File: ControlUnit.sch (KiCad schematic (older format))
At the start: 51 parts, among them SW1 SW_Push-Switch, U19 7400, U20 74LS161-74xx, U21 AT28C256, U22 AT28C256, U23 74LS138, U24 74LS138, U25 74LS138

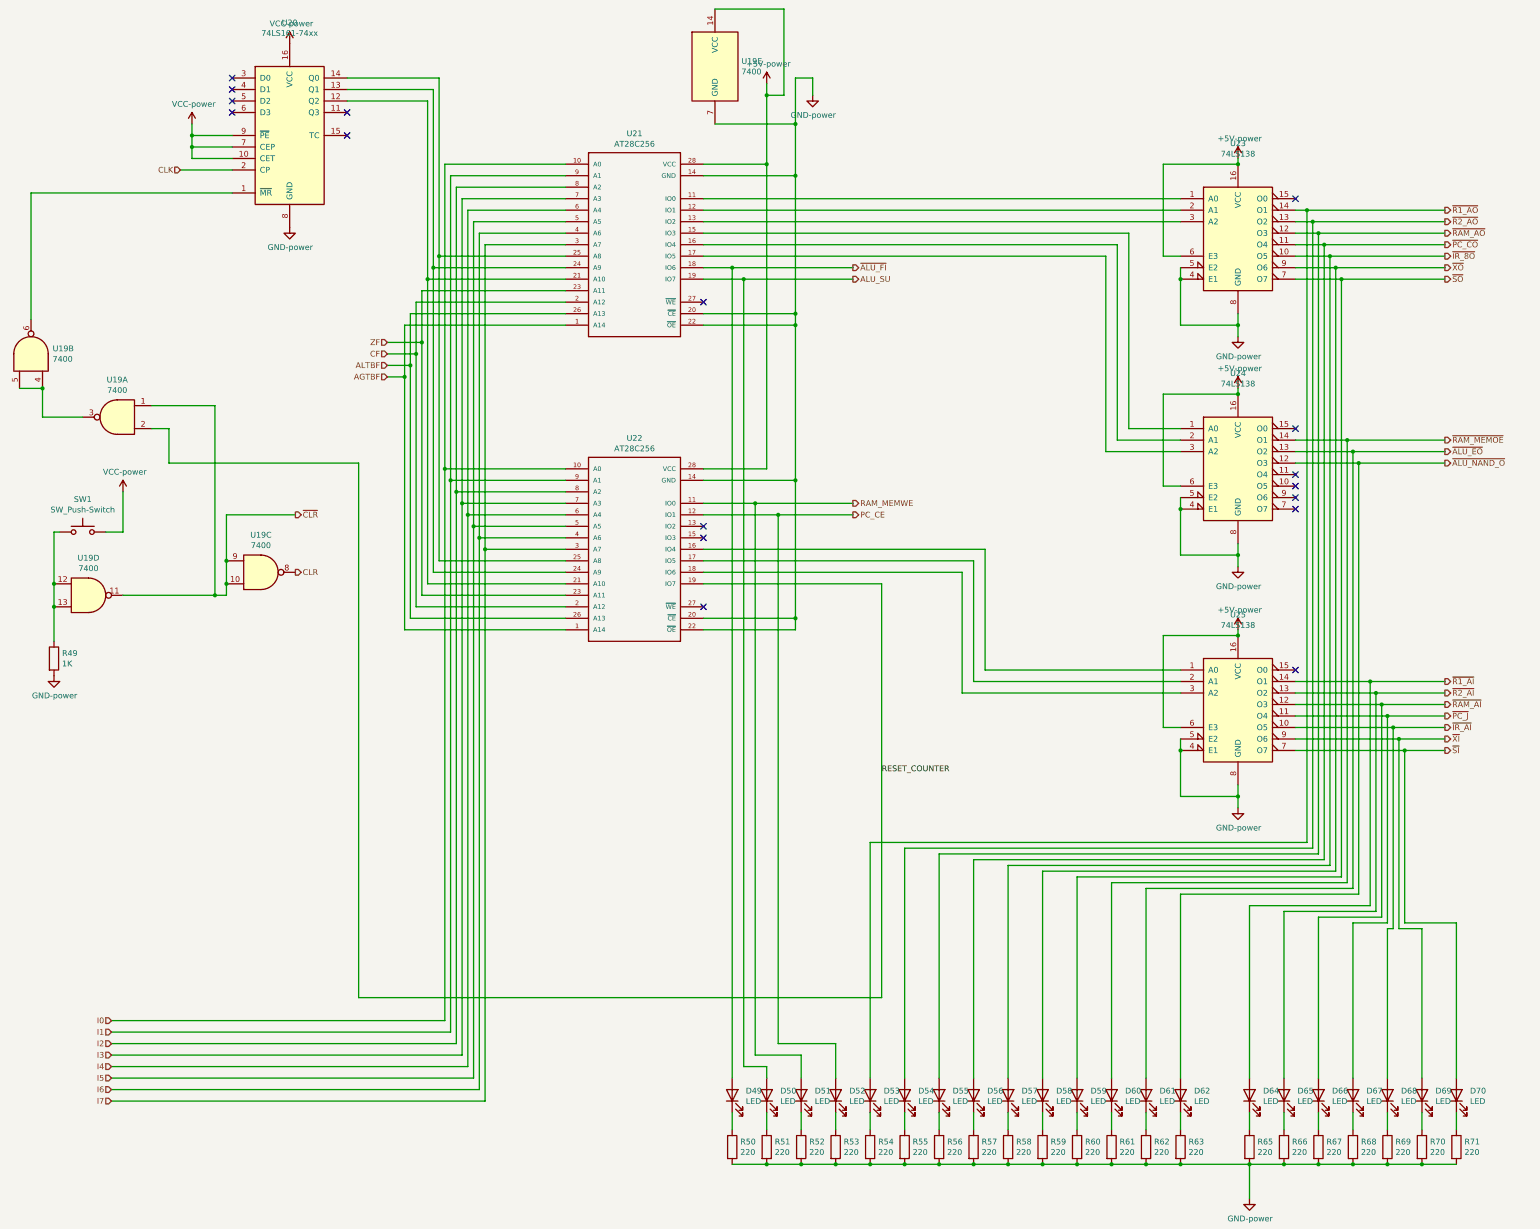
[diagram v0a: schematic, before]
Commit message: added images,fixed readme,renamed stuff to not include spaces
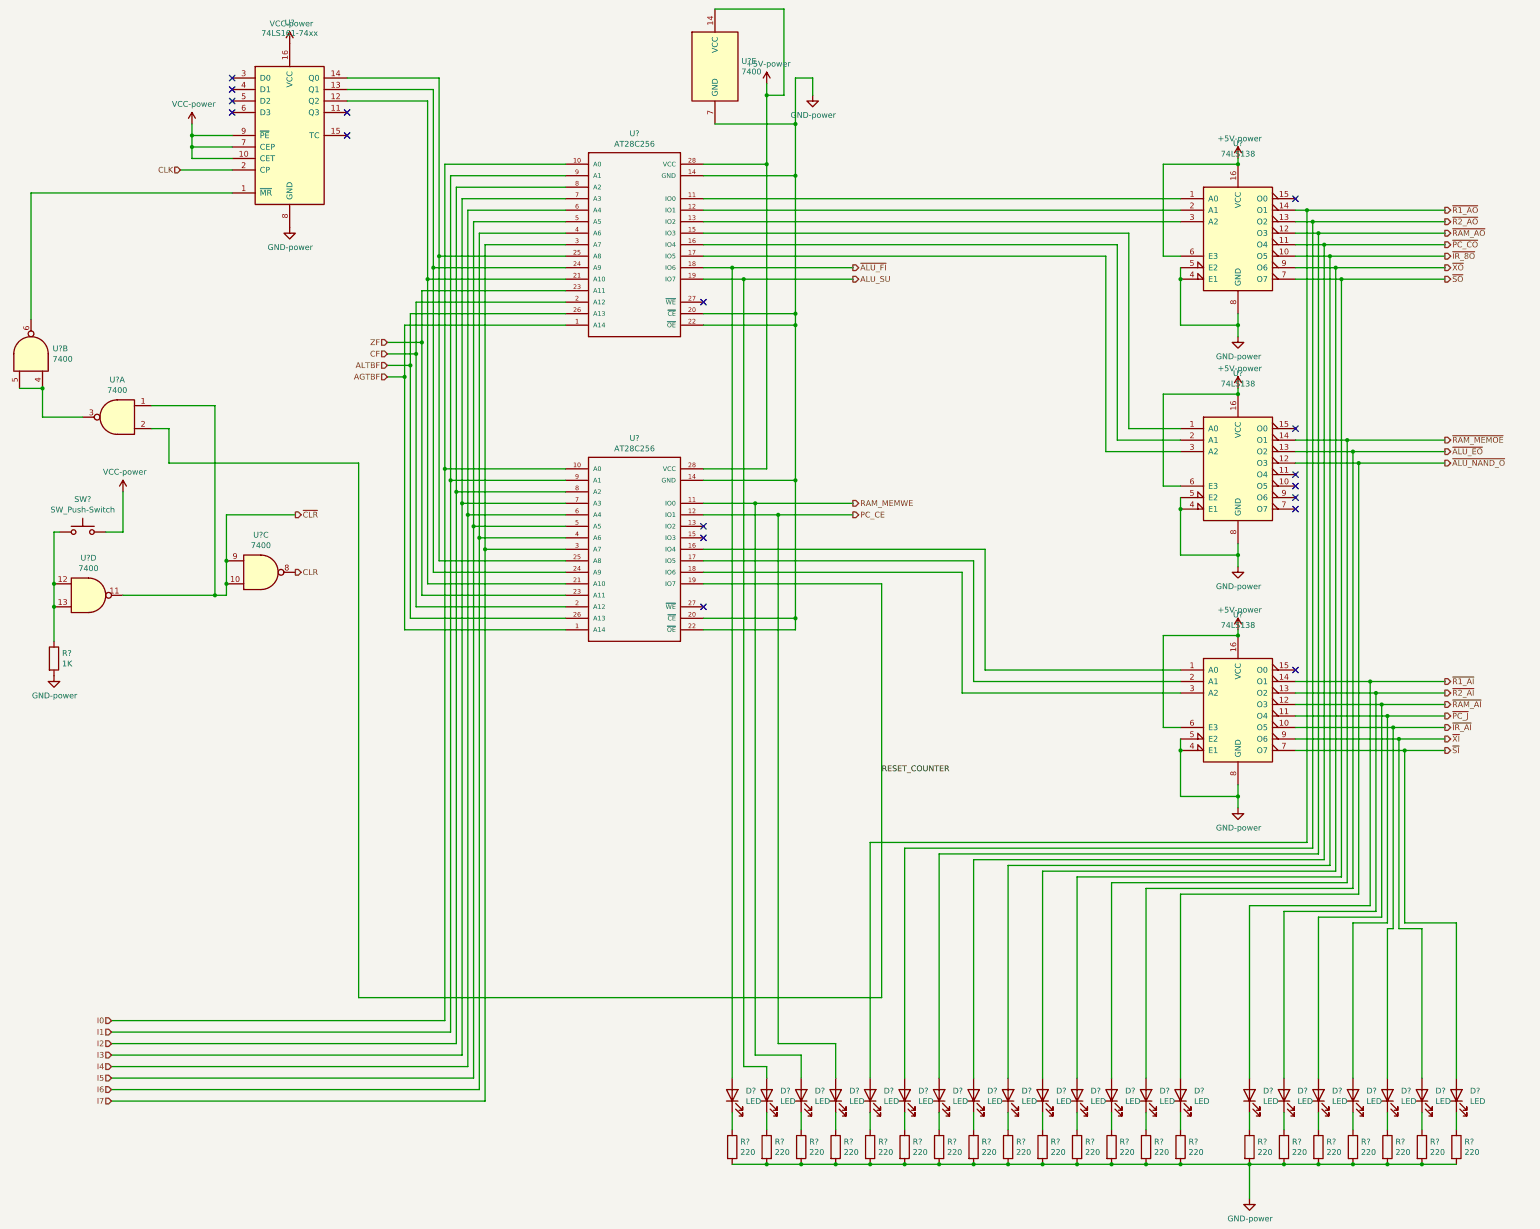
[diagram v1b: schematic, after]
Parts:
- renumbered R49 to R?, SW1 to SW?, U20 to U?, U19 to U?, U21 to U?, U22 to U?, U23 to U?, U25 to U?, U24 to U?

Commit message: added power caps
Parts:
- added C28, C29, C30, C31: 0.1uF, Capacitor_THT:CP_Axial_L10.0mm_D4.5mm_P15.00mm_Horizontal, symbol Device:C
- gave numbers to parts that had none: 9
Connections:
- net GND: now also C28.2, C29.2, C30.2, C31.2
- net VCC: now also C28.1, C29.1, C30.1, C31.1

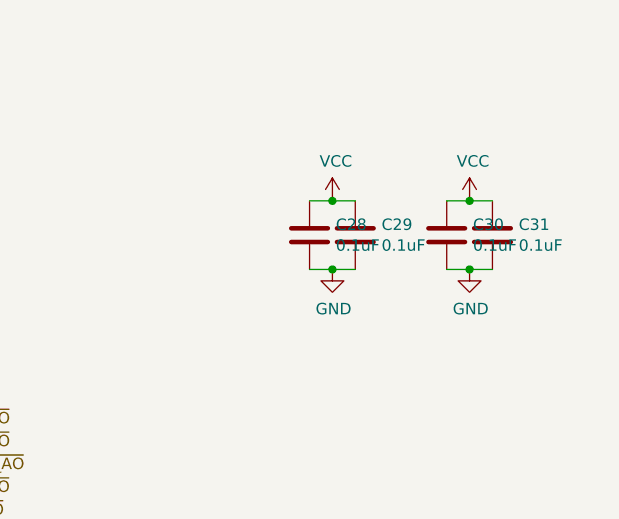
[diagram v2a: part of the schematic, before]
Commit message: Added power connector
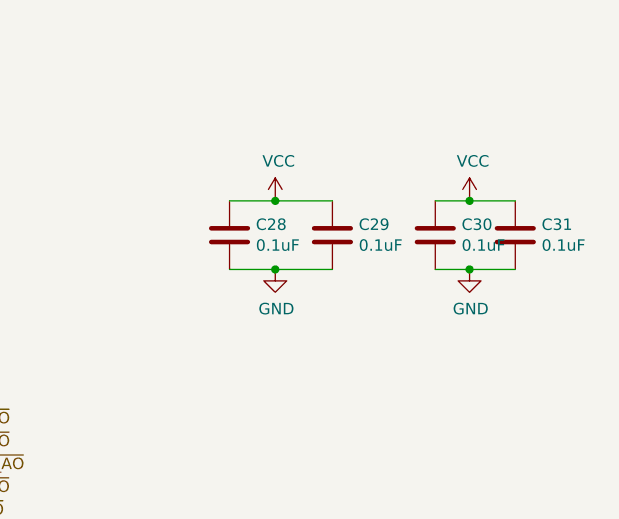
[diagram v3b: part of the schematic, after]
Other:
- moved on the sheet: C28, C29, C30, C31
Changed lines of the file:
@@
 $Descr A2 23386 16535
 encoding utf-8
-Sheet 21 21
+Sheet 21 22
 Title ""
 Date ""
@@
 L 16bitCpu-rescue:VCC-power #PWR?
 U 1 1 5FD5AD5A
-P 15300 1750
+P 15050 1750
 AR Path="/5FD5AD5A" Ref="#PWR?"  Part="1"
 AR Path="/5FD099BF/5FD5AD5A" Ref="#PWR0294"  Part="1"
-F 0 "#PWR0294" H 15300 1600 50  0001 C CNN
-F 1 "VCC" H 15315 1923 50  0000 C CNN
-F 2 "" H 15300 1750 50  0001 C CNN
-F 3 "" H 15300 1750 50  0001 C CNN
-	1    15300 1750
+F 0 "#PWR0294" H 15050 1600 50  0001 C CNN
+F 1 "VCC" H 15065 1923 50  0000 C CNN
+F 2 "" H 15050 1750 50  0001 C CNN
+F 3 "" H 15050 1750 50  0001 C CNN
+	1    15050 1750
 	1    0    0    -1
 $EndComp
@@
 L 16bitCpu-rescue:GND-power #PWR?
 U 1 1 5FD5AD60
-P 15300 2050
+P 15050 2050
 AR Path="/5FD5AD60" Ref="#PWR?"  Part="1"
 AR Path="/5F75E433/5FD5AD60" Ref="#PWR?"  Part="1"
 AR Path="/5FD099BF/5FD5AD60" Ref="#PWR0295"  Part="1"
-F 0 "#PWR0295" H 15300 1800 50  0001 C CNN
-F 1 "GND" H 15305 1877 50  0000 C CNN
-F 2 "" H 15300 2050 50  0001 C CNN
-F 3 "" H 15300 2050 50  0001 C CNN
-	1    15300 2050
-	1    0    0    -1
-$EndComp
-Wire Wire Line
-	15300 1750 15400 1750
-Wire Wire Line
-	15400 2050 15300 2050
+F 0 "#PWR0295" H 15050 1800 50  0001 C CNN
+F 1 "GND" H 15055 1877 50  0000 C CNN
+F 2 "" H 15050 2050 50  0001 C CNN
+F 3 "" H 15050 2050 50  0001 C CNN
+	1    15050 2050
+	1    0    0    -1
+$EndComp
 $Comp
 L Device:C C?
 U 1 1 5FD5AD68
-P 15200 1900
+P 14850 1900
 AR Path="/5F75E433/5FD5AD68" Ref="C?"  Part="1"
 AR Path="/5FD099BF/5FD5AD68" Ref="C28"  Part="1"
-F 0 "C28" H 15315 1946 50  0000 L CNN
-F 1 "0.1uF" H 15315 1855 50  0000 L CNN
-F 2 "Capacitor_THT:CP_Axial_L10.0mm_D4.5mm_P15.00mm_Horizontal" H 15238 1750 50  0001 C CNN
-F 3 "" H 15200 1900 50  0001 C CNN
-	1    15200 1900
-	1    0    0    -1
-$EndComp
-Wire Wire Line
-	15300 1750 15200 1750
-Connection ~ 15300 1750
-Wire Wire Line
-	15200 2050 15300 2050
-Connection ~ 15300 2050
+F 0 "C28" H 14965 1946 50  0000 L CNN
+F 1 "0.1uF" H 14965 1855 50  0000 L CNN
+F 2 "Capacitor_THT:CP_Axial_L10.0mm_D4.5mm_P15.00mm_Horizontal" H 14888 1750 50  0001 C CNN
+F 3 "" H 14850 1900 50  0001 C CNN
+	1    14850 1900
+	1    0    0    -1
+$EndComp
+Connection ~ 15050 1750
+Connection ~ 15050 2050
 $Comp
 L Device:C C?
 U 1 1 5FD5AD72
-P 15400 1900
+P 15300 1900
 AR Path="/5F75E433/5FD5AD72" Ref="C?"  Part="1"
 AR Path="/5FD099BF/5FD5AD72" Ref="C29"  Part="1"
-F 0 "C29" H 15515 1946 50  0000 L CNN
-F 1 "0.1uF" H 15515 1855 50  0000 L CNN
-F 2 "Capacitor_THT:CP_Axial_L10.0mm_D4.5mm_P15.00mm_Horizontal" H 15438 1750 50  0001 C CNN
-F 3 "" H 15400 1900 50  0001 C CNN
-	1    15400 1900
+F 0 "C29" H 15415 1946 50  0000 L CNN
+F 1 "0.1uF" H 15415 1855 50  0000 L CNN
+F 2 "Capacitor_THT:CP_Axial_L10.0mm_D4.5mm_P15.00mm_Horizontal" H 15338 1750 50  0001 C CNN
+F 3 "" H 15300 1900 50  0001 C CNN
+	1    15300 1900
 	1    0    0    -1
 $EndComp
@@
 	1    0    0    -1
 $EndComp
-Wire Wire Line
-	15900 1750 16000 1750
-Wire Wire Line
-	16000 2050 15900 2050
 $Comp
 L Device:C C?
 U 1 1 5FD78AFF
-P 15800 1900
+P 15750 1900
 AR Path="/5F75E433/5FD78AFF" Ref="C?"  Part="1"
 AR Path="/5FD099BF/5FD78AFF" Ref="C30"  Part="1"
-F 0 "C30" H 15915 1946 50  0000 L CNN
-F 1 "0.1uF" H 15915 1855 50  0000 L CNN
-F 2 "Capacitor_THT:CP_Axial_L10.0mm_D4.5mm_P15.00mm_Horizontal" H 15838 1750 50  0001 C CNN
-F 3 "" H 15800 1900 50  0001 C CNN
-	1    15800 1900
-	1    0    0    -1
-$EndComp
-Wire Wire Line
-	15900 1750 15800 1750
+F 0 "C30" H 15865 1946 50  0000 L CNN
+F 1 "0.1uF" H 15865 1855 50  0000 L CNN
+F 2 "Capacitor_THT:CP_Axial_L10.0mm_D4.5mm_P15.00mm_Horizontal" H 15788 1750 50  0001 C CNN
+F 3 "" H 15750 1900 50  0001 C CNN
+	1    15750 1900
+	1    0    0    -1
+$EndComp
 Connection ~ 15900 1750
-Wire Wire Line
-	15800 2050 15900 2050
 Connection ~ 15900 2050
 $Comp
 L Device:C C?
 U 1 1 5FD78B09
-P 16000 1900
+P 16100 1900
 AR Path="/5F75E433/5FD78B09" Ref="C?"  Part="1"
 AR Path="/5FD099BF/5FD78B09" Ref="C31"  Part="1"
-F 0 "C31" H 16115 1946 50  0000 L CNN
-F 1 "0.1uF" H 16115 1855 50  0000 L CNN
-F 2 "Capacitor_THT:CP_Axial_L10.0mm_D4.5mm_P15.00mm_Horizontal" H 16038 1750 50  0001 C CNN
-F 3 "" H 16000 1900 50  0001 C CNN
-	1    16000 1900
-	1    0    0    -1
-$EndComp
+F 0 "C31" H 16215 1946 50  0000 L CNN
+F 1 "0.1uF" H 16215 1855 50  0000 L CNN
+F 2 "Capacitor_THT:CP_Axial_L10.0mm_D4.5mm_P15.00mm_Horizontal" H 16138 1750 50  0001 C CNN
+F 3 "" H 16100 1900 50  0001 C CNN
+	1    16100 1900
+	1    0    0    -1
+$EndComp
+Wire Wire Line
+	15750 1750 15900 1750
+Wire Wire Line
+	15750 2050 15900 2050
+Wire Wire Line
+	15900 2050 16100 2050
+Wire Wire Line
+	15900 1750 16100 1750
+Wire Wire Line
+	15050 1750 15300 1750
+Wire Wire Line
+	15050 2050 15300 2050
+Wire Wire Line
+	14850 1750 15050 1750
+Wire Wire Line
+	14850 2050 15050 2050
 $EndSCHEMATC
